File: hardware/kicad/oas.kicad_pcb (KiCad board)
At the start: 2 copper layers, 120 x 103.5 mm, 69 parts, among them J1 Phoenix_MSTBA_2,5/3-G-5,08 (2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, J10 Native-USB recovery (DNP), J2 UART/Boot Recovery (DNP), J3 JST SM06B-GHS-TB (SEN66 conne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, J4 1x5 P1.27mm header (HLK-LD241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, J5 ESP32 row A (pins 1..15, ante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, J6 ESP32 row B (pins 16..30, USB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, J7 MIKROE mikroBUS pins 1..8 (AN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, J8 MIKROE mikroBUS pins 9..16 (P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, J9 JST SM04B-SRSS-TB (Qwiic / St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, Q1 AO3401A, SW1 C&K PTS645VK392LFS, U1 LM2596S-5.0, U2 TPS62933

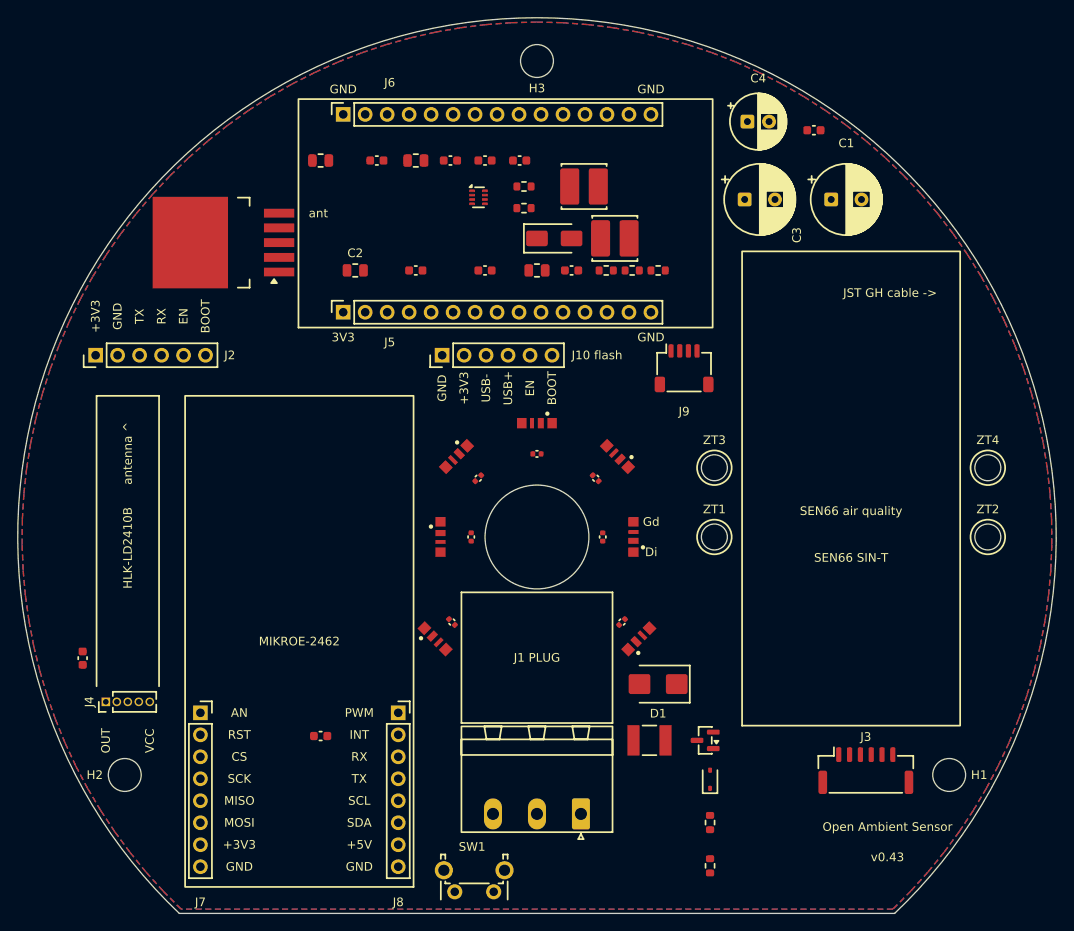
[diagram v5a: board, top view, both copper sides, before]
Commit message: feat(routing): v0.50 full routing rework — Freerouting + grid-A* + GND stitch
Complete re-route of the de-congested v0.50 placement. The board goes
from 89 unrouted ratsnest connections to a fully-connected board:
DRC 0 violations / 0 unconnected, ERC 0, determinism 20/20, build 30/30.

- Freerouting 2.2.4 (headless, Docker/Java 25) auto-routed 87 of 89
  nets on the 2-layer board from the placement baseline.
- The 2 nets Freerouting could not close (/IO/BTN J5.8->SW1.1 and
  Earth_Protective J1.3->C2.1, both long cross-board runs past the
  central cable hole) were closed with an obstacle-aware grid A*
  router.
- Two Freerouting cable-hole copper_edge_clearance issues fixed:
  /MCU/WS2812_DIN via relocated radially clear of the hole,
  /IO/I2C_SDA grazing segment ripped and A*-rerouted.
- F.Cu GND pour fragments stitched to the B.Cu GND plane: per-pad
  track+via stitches for stranded SMD GND pads, plus island stitches.
  Final stranded island located via the pcbnew-connectivity oracle.
- ROUTING_CHUNKS = ("gnd", "autoroute"); oas_routes.py holds the
  609-record snapshot (segments + vias).
- tools/extract_routes.py: fixed a parser bug — it required the
  quoted `(net N "name")` form and silently emitted 0 records from
  boardgen's bare `(net N)` tracks. Now resolves bare codes via the
  PCB header net table.
- pipeline/generic/03_drc.py: EXPECTED_UNCONNECTED 89 -> 0 (routing
  rework complete).

Known follow-up: JLCDFM PCB DFM shows polish items on the new vias
(0.15 mm annular rings, silkscreen-over-via, solder-mask clearances)
to be cleared next. SMT DFM 0/0.

Co-Authored-By: Claude Opus 4.7 <noreply@anthropic.com>
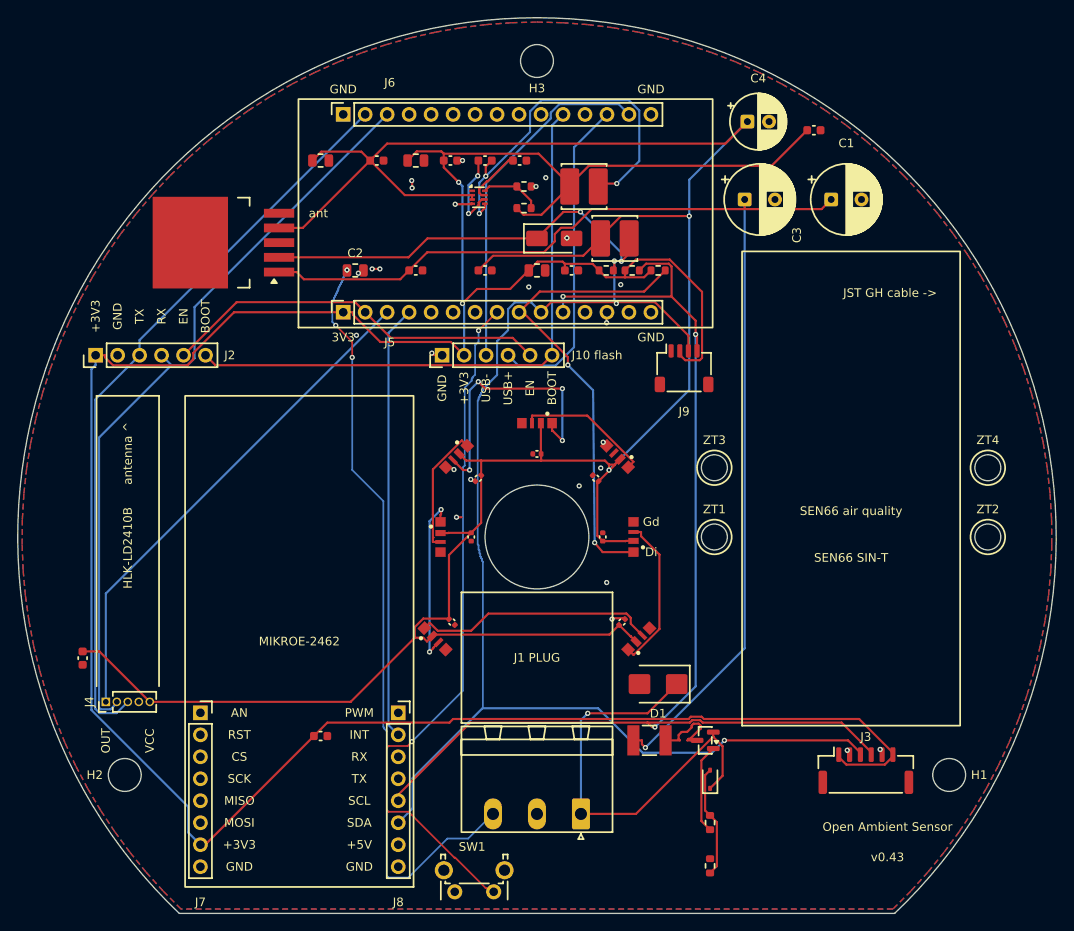
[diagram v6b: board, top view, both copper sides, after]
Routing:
- net +3V3: track 0.00 -> 337.5 mm, vias 0 -> 2
- net +5V: track 0.00 -> 292.7 mm, vias 0 -> 2
- net /IO/I2C_SDA: track 0.00 -> 144.2 mm, vias 0 -> 3
- net +24V: track 0.00 -> 139.7 mm, vias 0 -> 1
- net /IO/I2C_SCL: track 0.00 -> 138.7 mm, vias 0 -> 3
- net Earth_Protective: track 0.00 -> 88.9 mm, vias 0 -> 3
- net /MCU/UART_RX: track 0.00 -> 87.6 mm
- net /MCU/UART_TX: track 0.00 -> 86.1 mm
- net /IO/BTN: track 0.00 -> 80.4 mm, vias 0 -> 2
- net /IO/BOOT: track 0.00 -> 69.4 mm
- net /MCU/LD2410_OUT: track 0.00 -> 58.5 mm
- net /MCU/WS2812_DIN: track 0.00 -> 54.3 mm, vias 0 -> 2
- net /MCU/NFC_FD: track 0.00 -> 50.3 mm
- net Net-(D1-K): track 0.00 -> 50.2 mm, vias 0 -> 1
- net Net-(D2-K): track 0.00 -> 47.7 mm, vias 0 -> 2
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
